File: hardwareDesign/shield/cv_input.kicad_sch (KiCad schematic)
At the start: 39 parts, among them J3 WQP419, J5 WQP419, J6 WQP419, J7 WQP419, J8 WQP419, J9 WQP419, U3 TLV9062, U4 TLV9062, U5 TLV9062

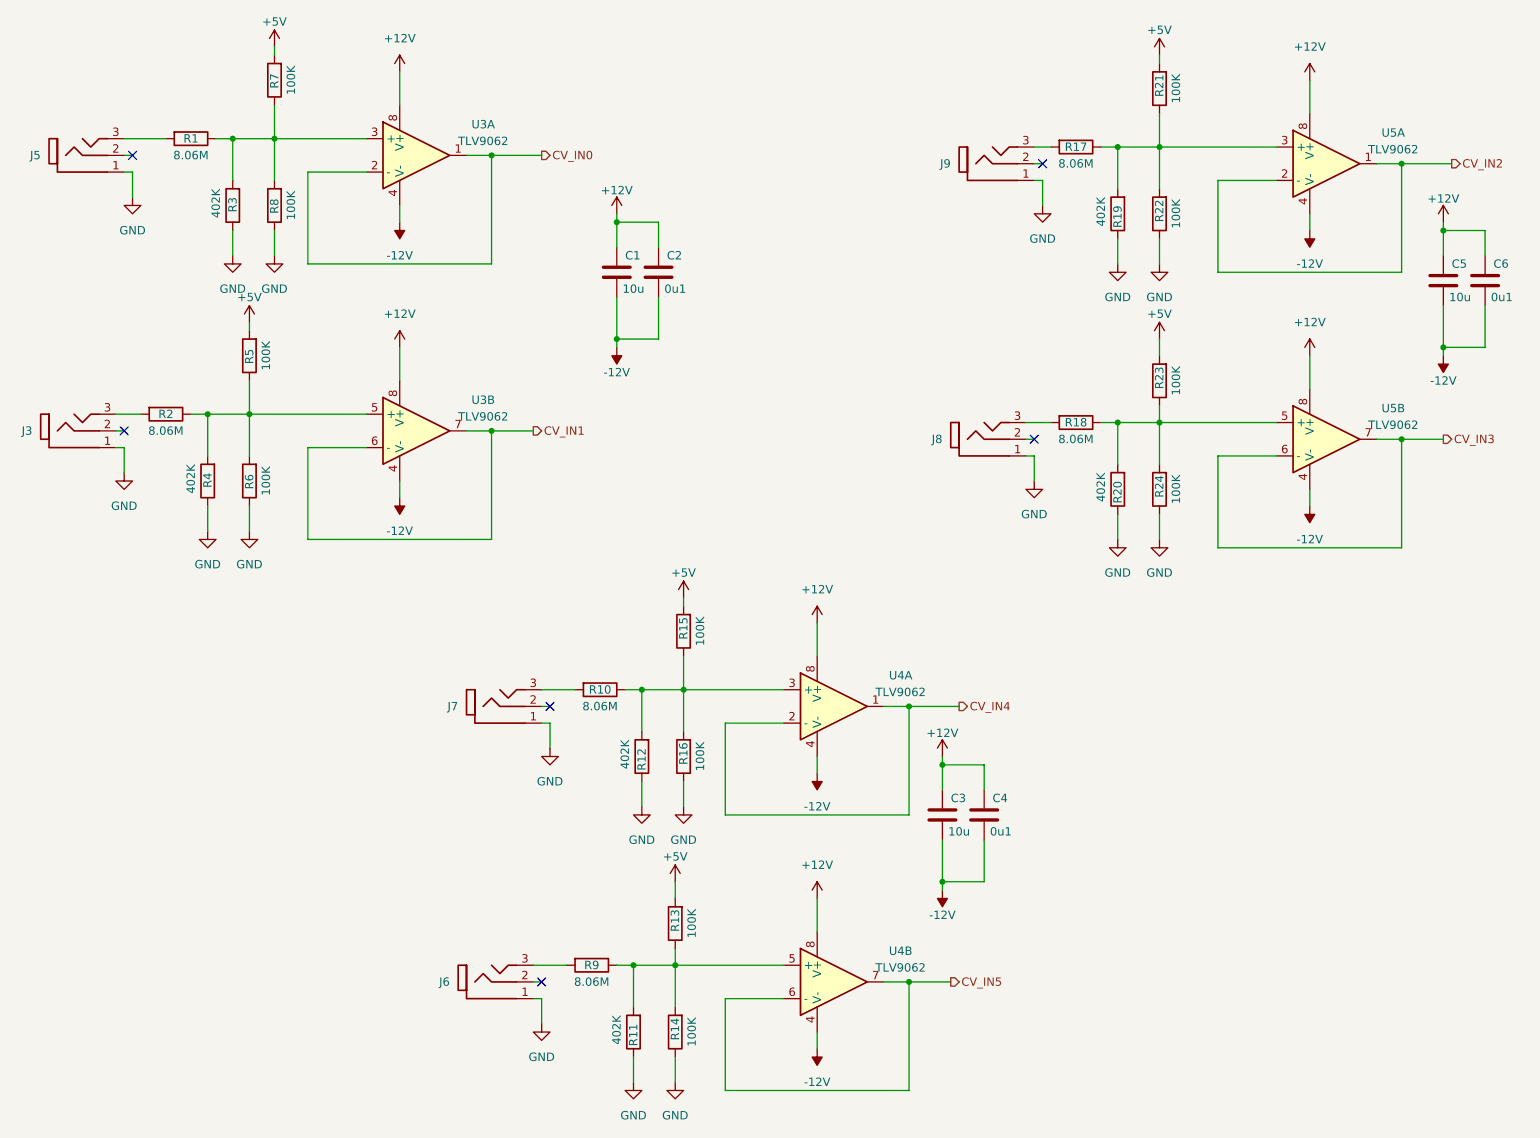
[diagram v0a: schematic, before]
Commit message: Finished schematic and PCB for jetson Nano Sheild
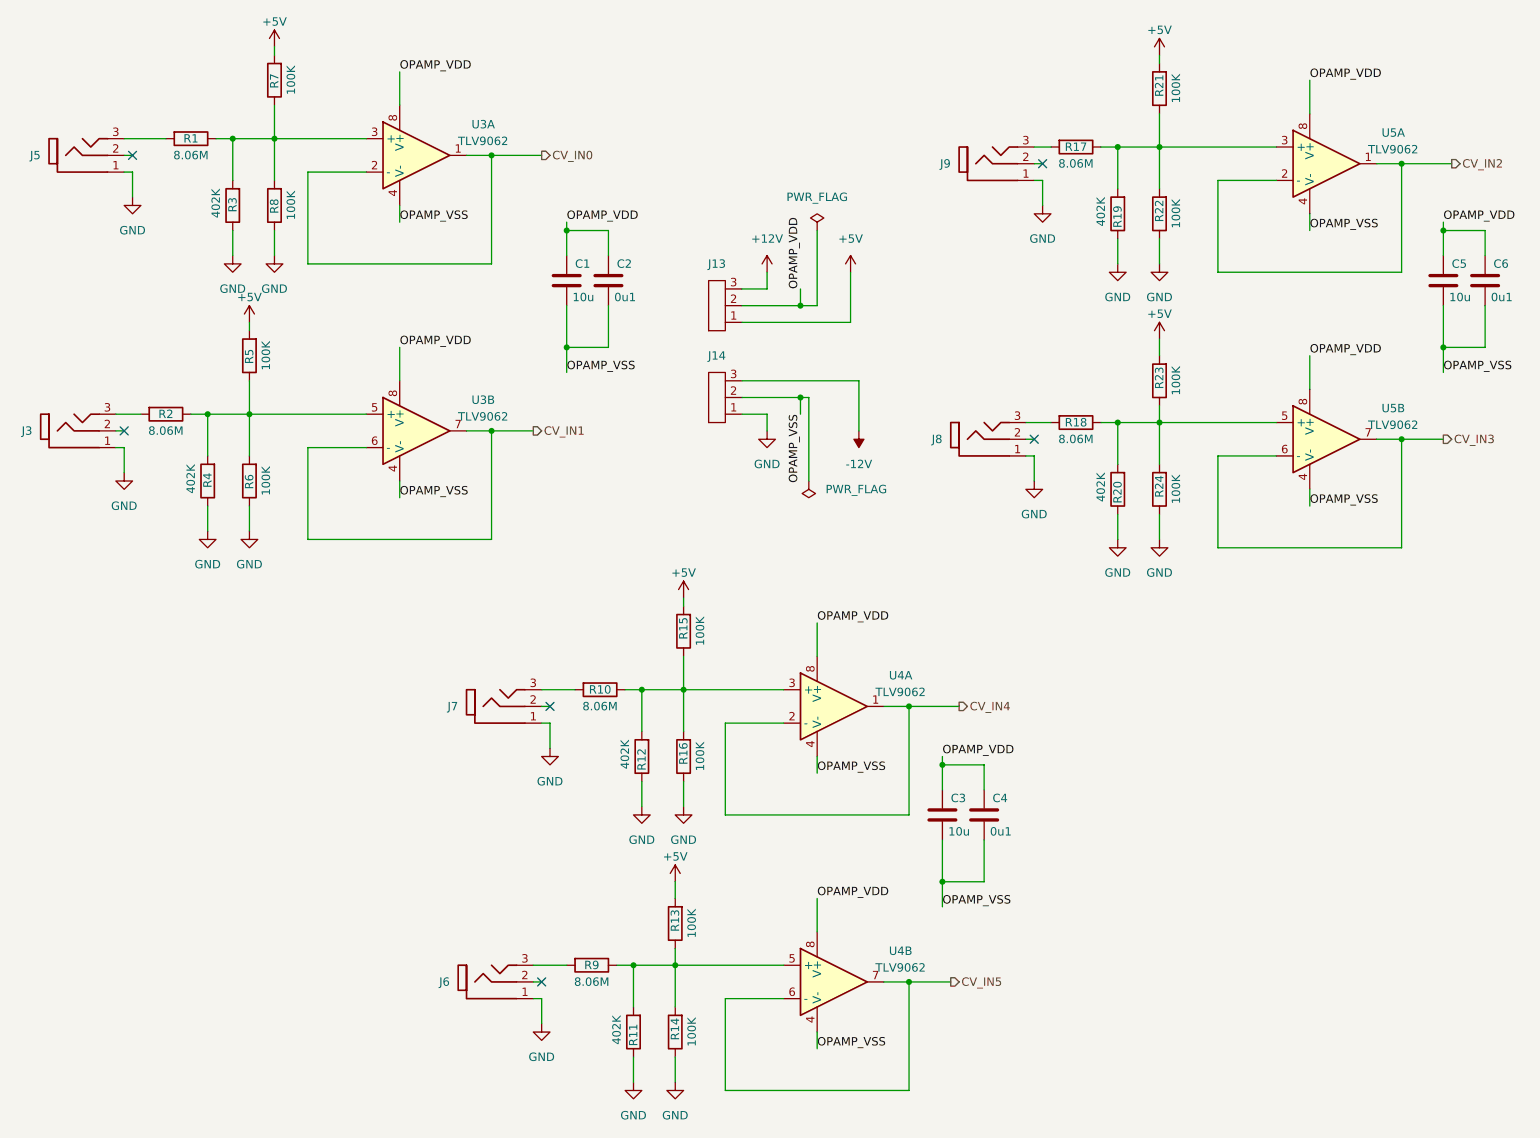
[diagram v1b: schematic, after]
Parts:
- added J13, J14: 3x1_PIN_HEADER, connectors:03x01_2.54_pitch_pin_header, symbol connectors:3x1_PIN_HEADER
- U3, U4, U5: footprint ti:TL072_SOIC-8 -> SOT:SOT23-8
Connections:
- net +12V: now also J13.3; no longer C1.1, C2.1, C3.1, C4.1, C5.1, C6.1, U3.8 (V+), U3.8 (V+), U4.8 (V+), U4.8 (V+), U5.8 (V+), U5.8 (V+)
- net +5V: now also J13.1
- net -12V: now also J14.3; no longer C1.2, C2.2, C3.2, C4.2, C5.2, C6.2, U3.4 (V-), U3.4 (V-), U4.4 (V-), U4.4 (V-), U5.4 (V-), U5.4 (V-)
- net GND: now also J14.1
- new net OPAMP_VDD: C1.1, C2.1, C3.1, C4.1, C5.1, C6.1, J13.2, U3.8 (V+), U3.8 (V+), U4.8 (V+), U4.8 (V+), U5.8 (V+), U5.8 (V+)
- new net OPAMP_VSS: C1.2, C2.2, C3.2, C4.2, C5.2, C6.2, J14.2, U3.4 (V-), U3.4 (V-), U4.4 (V-), U4.4 (V-), U5.4 (V-), U5.4 (V-)
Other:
- moved on the sheet: C1, C2
